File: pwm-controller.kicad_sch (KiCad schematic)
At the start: 41 parts, among them J1 DEBUG_ADDRESS_I2C_INT, J2 POWER, J3 OUT+, J4 OUT-, SW1 EC12D1524403, U1 STM8S003F3Px, U2 78L05

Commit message: order files
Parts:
- renumbered C4 to C1, C14 to C10, C5 to C2, C7 to C4, C8 to C5, C9 to C6, C2 to C7, C1 to C8, C6 to C9, D2 to D1, D1 to D2, H4 to H2, H2 to H3, H5 to H4, H7 to H5, H3 to H6, H6 to H7, J2 to J1, J1 to J2, R8 to R1, R7 to R10, R21 to R11, R10 to R2, R5 to R4, R9 to R5, R1 to R6, R2 to R7, R4 to R8, R6 to R9, U2 to U1, U1 to U2

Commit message: rendered some docs
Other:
- title: (none) -> Dual-channel PWM LED-strip controller
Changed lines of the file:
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@@
 (kicad_sch (version 20211123) (generator eeschema)
   (paper "A4")
+  (title_block
+    (title "Dual-channel PWM LED-strip controller")
+  )
   (junction (at 113.03 95.25) (diameter 0) (color 0 0 0 0)
   )

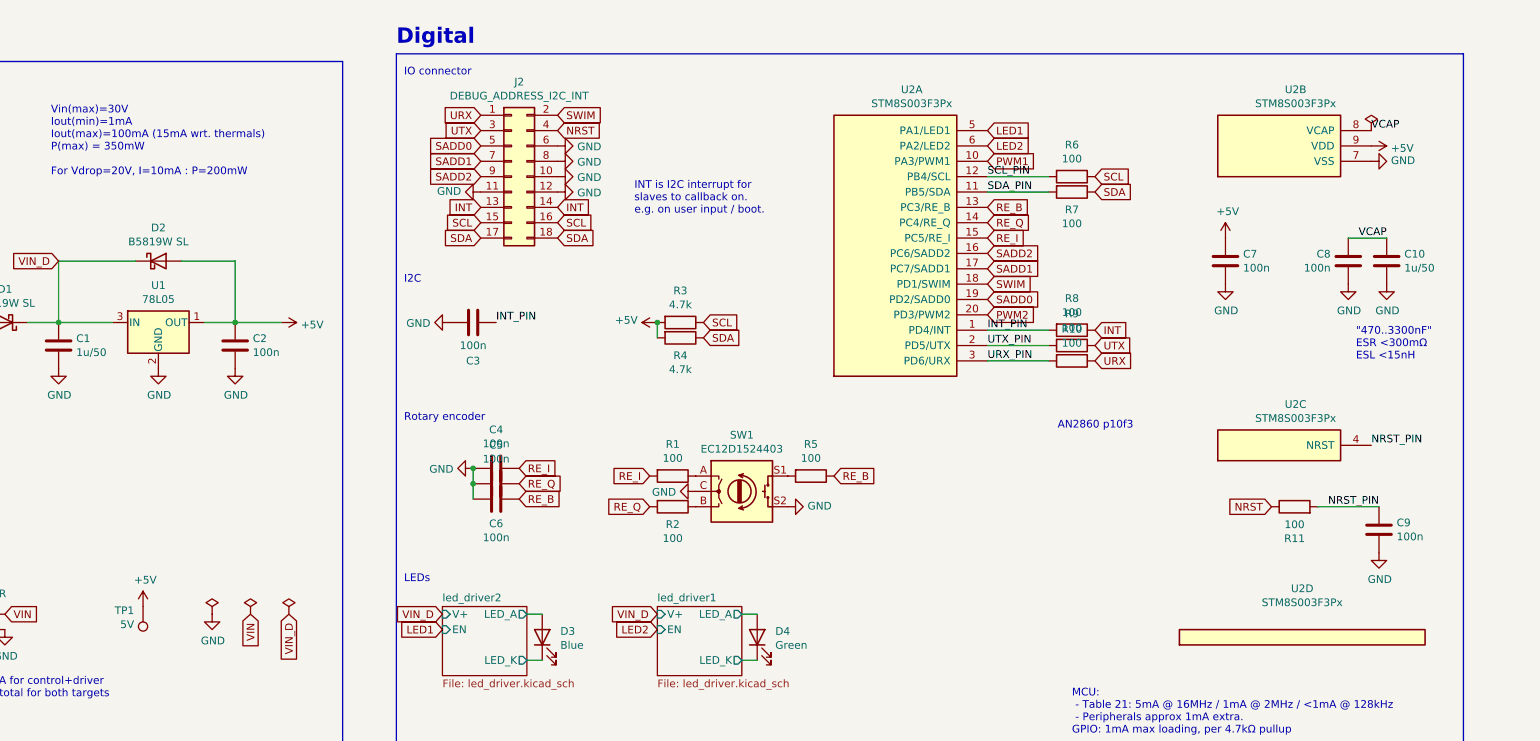
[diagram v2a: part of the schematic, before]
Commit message: fix rotary pinout, add 5v0 to header in extra-col, regen fab+doc
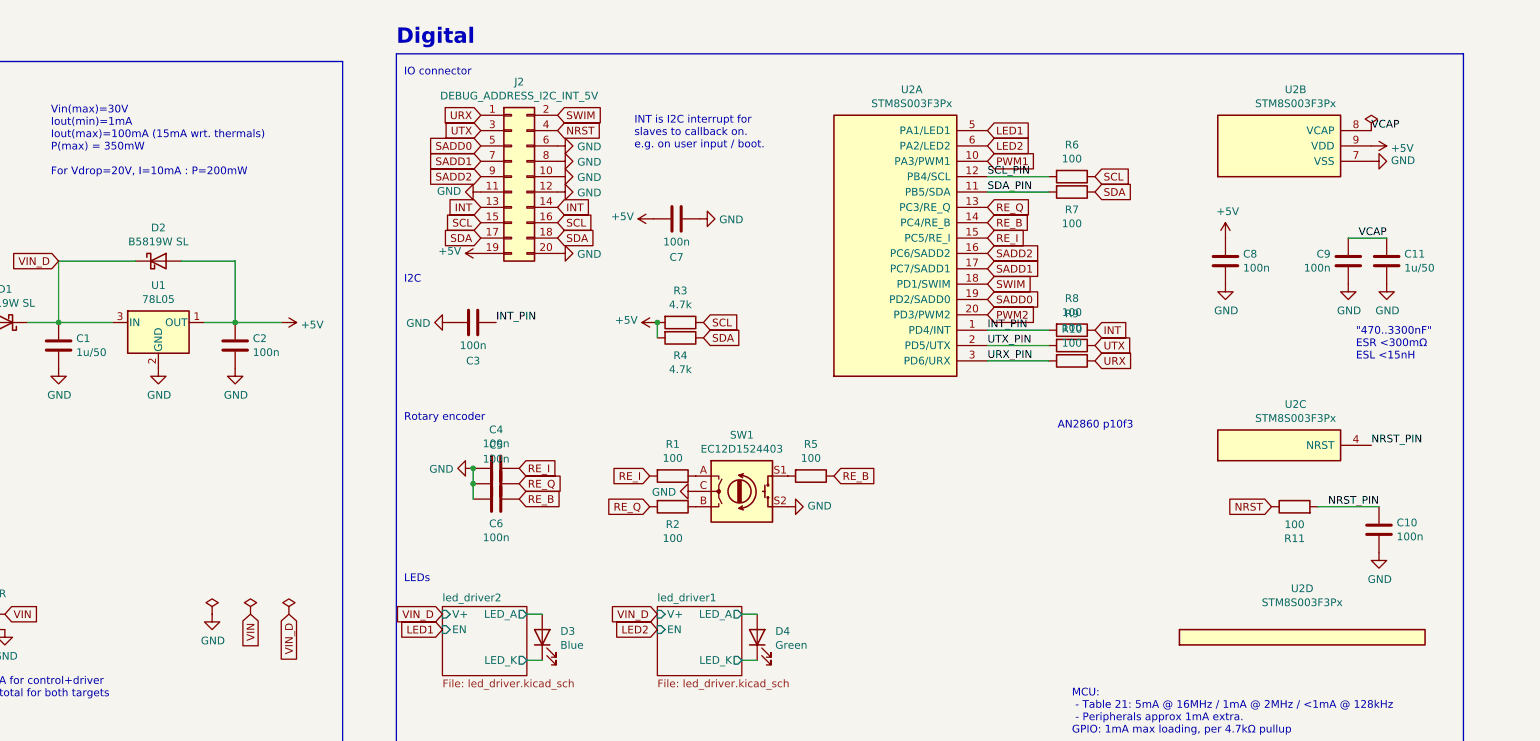
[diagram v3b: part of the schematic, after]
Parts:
- removed TP1: 5V, TestPoint:TestPoint_THTPad_D1.5mm_Drill0.7mm, symbol Connector:TestPoint
- added C7: 100n, Capacitor_SMD:C_0402_1005Metric, symbol Device:C
- J2: value DEBUG_ADDRESS_I2C_INT -> DEBUG_ADDRESS_I2C_INT_5V; footprint Connector_PinHeader_2.54mm:PinHeader_2x09_P2.54mm_Horizontal -> Connector_PinHeader_2.54mm:PinHeader_2x10_P2.54mm_Horizontal; symbol Connector_Generic:Conn_02x09_Odd_Even -> Connector_Generic:Conn_02x10_Odd_Even; JLC C492437 -> C492438
- renumbered C9 to C10, C10 to C11, C7 to C8, C8 to C9
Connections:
- net +5V: now also J2.19 (Pin_19), C7.1
- net GND: now also J2.20 (Pin_20), C7.2
- net RE_B: now also U2.14 (PC4/RE_B); no longer U2.13 (PC3/RE_B)
- net RE_Q: now also U2.13 (PC3/RE_Q); no longer U2.14 (PC4/RE_Q)

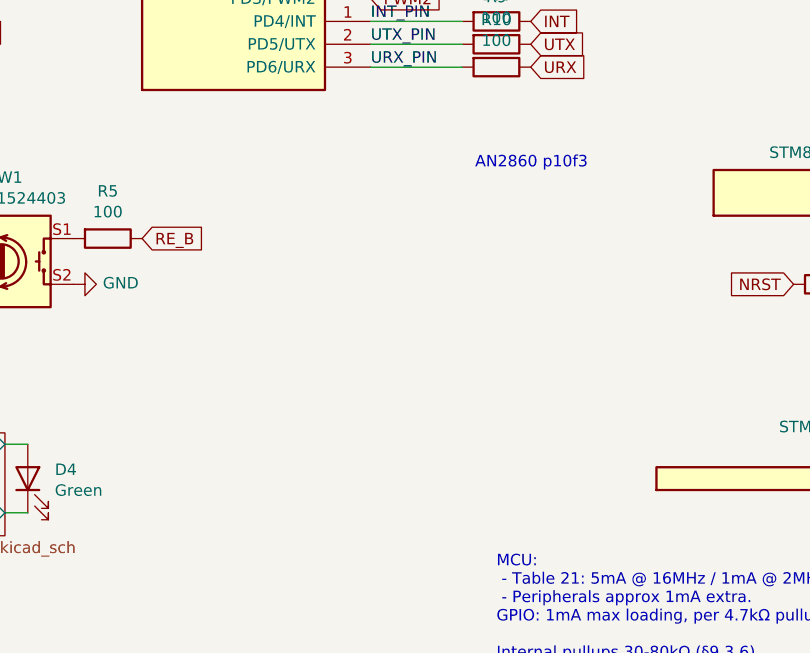
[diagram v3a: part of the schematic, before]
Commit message: TVS diodes added to I2C SDA+SCL+INT pins, renamed 1-/2- to A-/B-
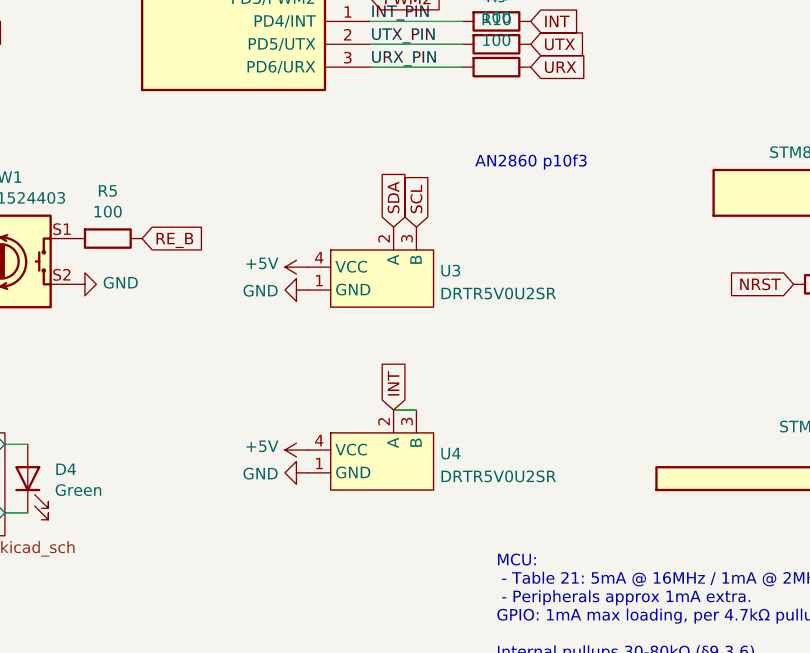
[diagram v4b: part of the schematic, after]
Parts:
- added U3, U4: DRTR5V0U2SR, Package_TO_SOT_SMD:SOT-143, symbol mark:DRTR5V0U2SR
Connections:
- net +5V: now also U3.4 (VCC), U4.4 (VCC)
- net GND: now also U3.1 (GND), U4.1 (GND)
- net INT: now also U4.2 (A), U4.3 (B)
- net SCL: now also U3.3 (B)
- net SDA: now also U3.2 (A)

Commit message: improvements, notes for future TODO stuff
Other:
- note added: "- ISO1540 to isolate I2C (need BUSPWR and BUSGND pins on connector) - Opto-isolator for INT? Perhaps move I2C+INT+BUSPWR+BUSGND to a pair of 5-pin JST connectors?"
- note added: "Should we add LC on input? 10A @ 1kHz : Q < 10 mC/cycle C=Q/V @ 12V : >1000μF L=1/(C 4π² f²) @ 1kHz & 1000uF : > 25μH Examples at bare-min spec: L = Bourns SRP1770C-330M (33μH, 18x17mm, €4) C = UC EKYC500ELL122ML20S (1200μF, 38mΩ, €2) L = Bourns SRP1265C-6R8M (6.8μH, 14x13mm, €2) C = Cornell SLPX103M050E7P3 (10mF, 46mΩ, €5) Ideally, we over-spec though, since capacitor discharge is not flat like 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"
- moved on the sheet: J1
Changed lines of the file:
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@@
+    (effects (font (size 1.27 1.27)) (justify left bottom))
+  )
+  (text "Should we add LC on input?\n\n10A @ 1kHz : Q < 10 mC/cycle\n\nC=Q/V @ 12V : >1000μF\n\nL=1/(C 4π² f²) @ 1kHz & 1000uF : > 25μH\n\nExamples at bare-min spec:\n\nL = Bourns SRP1770C-330M (33μH, 18x17mm, €4)\nC = UC EKYC500ELL122ML20S (1200μF, 38mΩ, €2)\n\nL = Bourns SRP1265C-6R8M (6.8μH, 14x13mm, €2)\nC = Cornell SLPX103M050E7P3 (10mF, 46mΩ, €5)\n\nIdeally, we over-spec though, since capacitor discharge is not flat like LiPo..."
+    (at -87.63 118.745 0)
+    (effects (font (size 1.27 1.27)) (justify left bottom))
+  )
+  (text " - ISO1540 to isolate I2C (need BUSPWR and BUSGND pins on connector)\n - Opto-isolator for INT?\n\nPerhaps move I2C+INT+BUSPWR+BUSGND to a pair of 5-pin JST connectors?"
+    (at 300.99 111.125 0)
     (effects (font (size 1.27 1.27)) (justify left bottom))
   )
@@
   )
   (text "<10mA for control+driver\n<15A total for both targets"
-    (at 29.21 130.81 0)
+    (at 29.21 113.665 0)
     (effects (font (size 1.27 1.27)) (justify left bottom))
   )
@@
     )
   )
-  (global_label "VIN_D" (shape input) (at 82.55 116.84 270) (fields_autoplaced)
-    (effects (font (size 1.27 1.27)) (justify right))
-    (property "Intersheet References" "${INTERSHEET_REFS}" (id 0) (at 0 0 0)
+  (global_label "VIN_D" (shape input) (at 82.55 99.695 270) (fields_autoplaced)
+    (effects (font (size 1.27 1.27)) (justify right))
+    (property "Intersheet References" "${INTERSHEET_REFS}" (id 0) (at 0 -17.145 0)
       (effects (font (size 1.27 1.27)) hide)
     )
@@
     )
   )
-  (global_label "VIN" (shape input) (at 76.2 116.84 270) (fields_autoplaced)
-    (effects (font (size 1.27 1.27)) (justify right))
-    (property "Intersheet References" "${INTERSHEET_REFS}" (id 0) (at 0 0 0)
+  (global_label "VIN" (shape input) (at 76.2 99.695 270) (fields_autoplaced)
+    (effects (font (size 1.27 1.27)) (justify right))
+    (property "Intersheet References" "${INTERSHEET_REFS}" (id 0) (at 0 -17.145 0)
       (effects (font (size 1.27 1.27)) hide)
     )
@@
     )
   )
-  (global_label "VIN" (shape input) (at 35.56 116.84 0) (fields_autoplaced)
-    (effects (font (size 1.27 1.27)) (justify left))
-    (property "Intersheet References" "${INTERSHEET_REFS}" (id 0) (at 0 0 0)
+  (global_label "VIN" (shape input) (at 35.56 99.695 0) (fields_autoplaced)
+    (effects (font (size 1.27 1.27)) (justify left))
+    (property "Intersheet References" "${INTERSHEET_REFS}" (id 0) (at 0 -17.145 0)
       (effects (font (size 1.27 1.27)) hide)
     )
@@
     (pin "2")
   )
-  (symbol (lib_id "power:PWR_FLAG") (at 76.2 116.84 0) (unit 1)
-    (in_bom yes) (on_board yes)
-    (property "Reference" "#FLG02" (id 0) (at 76.2 114.935 0)
-      (effects (font (size 1.27 1.27)) hide)
-    )
-    (property "Value" "PWR_FLAG" (id 1) (at 76.2 112.4458 0)
-      (effects (font (size 1.27 1.27)) hide)
-    )
-    (property "Footprint" "" (id 2) (at 76.2 116.84 0)
-      (effects (font (size 1.27 1.27)) hide)
-    )
-    (property "Datasheet" "~" (id 3) (at 76.2 116.84 0)
+  (symbol (lib_id "power:PWR_FLAG") (at 76.2 99.695 0) (unit 1)
+    (in_bom yes) (on_board yes)
+    (property "Reference" "#FLG02" (id 0) (at 76.2 97.79 0)
+      (effects (font (size 1.27 1.27)) hide)
+    )
+    (property "Value" "PWR_FLAG" (id 1) (at 76.2 95.3008 0)
+      (effects (font (size 1.27 1.27)) hide)
+    )
+    (property "Footprint" "" (id 2) (at 76.2 99.695 0)
+      (effects (font (size 1.27 1.27)) hide)
+    )
+    (property "Datasheet" "~" (id 3) (at 76.2 99.695 0)
       (effects (font (size 1.27 1.27)) hide)
     )
@@
     (pin "1")
   )
-  (symbol (lib_id "power:PWR_FLAG") (at 69.85 116.84 0) (unit 1)
-    (in_bom yes) (on_board yes)
-    (property "Reference" "#FLG01" (id 0) (at 69.85 114.935 0)
-      (effects (font (size 1.27 1.27)) hide)
-    )
-    (property "Value" "PWR_FLAG" (id 1) (at 69.85 112.4458 0)
-      (effects (font (size 1.27 1.27)) hide)
-    )
-    (property "Footprint" "" (id 2) (at 69.85 116.84 0)
-      (effects (font (size 1.27 1.27)) hide)
-    )
-    (property "Datasheet" "~" (id 3) (at 69.85 116.84 0)
+  (symbol (lib_id "power:PWR_FLAG") (at 69.85 99.695 0) (unit 1)
+    (in_bom yes) (on_board yes)
+    (property "Reference" "#FLG01" (id 0) (at 69.85 97.79 0)
+      (effects (font (size 1.27 1.27)) hide)
+    )
+    (property "Value" "PWR_FLAG" (id 1) (at 69.85 95.3008 0)
+      (effects (font (size 1.27 1.27)) hide)
+    )
+    (property "Footprint" "" (id 2) (at 69.85 99.695 0)
+      (effects (font (size 1.27 1.27)) hide)
+    )
+    (property "Datasheet" "~" (id 3) (at 69.85 99.695 0)
       (effects (font (size 1.27 1.27)) hide)
     )
@@
     (pin "1")
   )
-  (symbol (lib_id "power:GND") (at 69.85 116.84 0) (unit 1)
-    (in_bom yes) (on_board yes)
-    (property "Reference" "#PWR04" (id 0) (at 69.85 123.19 0)
-      (effects (font (size 1.27 1.27)) hide)
-    )
-    (property "Value" "GND" (id 1) (at 69.977 121.2342 0))
-    (property "Footprint" "" (id 2) (at 69.85 116.84 0)
-      (effects (font (size 1.27 1.27)) hide)
-    )
-    (property "Datasheet" "" (id 3) (at 69.85 116.84 0)
+  (symbol (lib_id "power:GND") (at 69.85 99.695 0) (unit 1)
+    (in_bom yes) (on_board yes)
+    (property "Reference" "#PWR04" (id 0) (at 69.85 106.045 0)
+      (effects (font (size 1.27 1.27)) hide)
+    )
+    (property "Value" "GND" (id 1) (at 69.977 104.0892 0))
+    (property "Footprint" "" (id 2) (at 69.85 99.695 0)
+      (effects (font (size 1.27 1.27)) hide)
+    )
+    (property "Datasheet" "" (id 3) (at 69.85 99.695 0)
       (effects (font (size 1.27 1.27)) hide)
     )
@@
     (pin "1")
   )
-  (symbol (lib_id "Connector:Screw_Terminal_01x02") (at 30.48 119.38 180) (unit 1)
-    (in_bom yes) (on_board yes)
-    (property "Reference" "J1" (id 0) (at 32.5628 111.125 0))
-    (property "Value" "POWER" (id 1) (at 32.5628 113.4364 0))
-    (property "Footprint" "mark:ScrewTerminal_5.08P_1x02_10.16x10.16mm" (id 2) (at 30.48 119.38 0)
-      (effects (font (size 1.27 1.27)) hide)
-    )
-    (property "Datasheet" "https://datasheet.lcsc.com/lcsc/1912251636_Ningbo-Kangnex-Elec-WJ500V-5.08-2P_C8465.pdf" (id 3) (at 30.48 119.38 0)
-      (effects (font (size 1.27 1.27)) hide)
-    )
-    (property "JLC" "C8465" (id 4) (at 30.48 119.38 0)
-      (effects (font (size 1.27 1.27)) hide)
-    )
-    (pin "1")
-    (pin "2")
-  )
-  (symbol (lib_id "power:GND") (at 35.56 119.38 0) (unit 1)
-    (in_bom yes) (on_board yes)
-    (property "Reference" "#PWR01" (id 0) (at 35.56 125.73 0)
-      (effects (font (size 1.27 1.27)) hide)
-    )
-    (property "Value" "GND" (id 1) (at 35.687 123.7742 0))
-    (property "Footprint" "" (id 2) (at 35.56 119.38 0)
-      (effects (font (size 1.27 1.27)) hide)
-    )
-    (property "Datasheet" "" (id 3) (at 35.56 119.38 0)
+  (symbol (lib_id "Connector:Screw_Terminal_01x02") (at 30.48 102.235 180) (unit 1)
+    (in_bom yes) (on_board yes)
+    (property "Reference" "J1" (id 0) (at 32.5628 93.98 0))
+    (property "Value" "POWER" (id 1) (at 32.5628 96.2914 0))
+    (property "Footprint" "mark:ScrewTerminal_5.08P_1x02_10.16x10.16mm" (id 2) (at 30.48 102.235 0)
+      (effects (font (size 1.27 1.27)) hide)
+    )
+    (property "Datasheet" "https://datasheet.lcsc.com/lcsc/1912251636_Ningbo-Kangnex-Elec-WJ500V-5.08-2P_C8465.pdf" (id 3) (at 30.48 102.235 0)
+      (effects (font (size 1.27 1.27)) hide)
+    )
+    (property "JLC" "C8465" (id 4) (at 30.48 102.235 0)
+      (effects (font (size 1.27 1.27)) hide)
+    )
+    (pin "1")
+    (pin "2")
+  )
+  (symbol (lib_id "power:GND") (at 35.56 102.235 0) (unit 1)
+    (in_bom yes) (on_board yes)
+    (property "Reference" "#PWR01" (id 0) (at 35.56 108.585 0)
+      (effects (font (size 1.27 1.27)) hide)
+    )
+    (property "Value" "GND" (id 1) (at 35.687 106.6292 0))
+    (property "Footprint" "" (id 2) (at 35.56 102.235 0)
+      (effects (font (size 1.27 1.27)) hide)
+    )
+    (property "Datasheet" "" (id 3) (at 35.56 102.235 0)
       (effects (font (size 1.27 1.27)) hide)
     )
@@
     (pin "2")
   )
-  (symbol (lib_id "power:PWR_FLAG") (at 82.55 116.84 0) (unit 1)
-    (in_bom yes) (on_board yes)
-    (property "Reference" "#FLG03" (id 0) (at 82.55 114.935 0)
-      (effects (font (size 1.27 1.27)) hide)
-    )
-    (property "Value" "PWR_FLAG" (id 1) (at 82.55 112.4458 0)
-      (effects (font (size 1.27 1.27)) hide)
-    )
-    (property "Footprint" "" (id 2) (at 82.55 116.84 0)
-      (effects (font (size 1.27 1.27)) hide)
-    )
-    (property "Datasheet" "~" (id 3) (at 82.55 116.84 0)
-      (effects (font (size 1.27 1.27)) hide)
-    )
+  (symbol (lib_id "power:PWR_FLAG") (at 82.55 99.695 0) (unit 1)
+    (in_bom yes) (on_board yes)
+    (property "Reference" "#FLG03" (id 0) (at 82.55 97.79 0)
+      (effects (font (size 1.27 1.27)) hide)
+    )
+    (property "Value" "PWR_FLAG" (id 1) (at 82.55 95.3008 0)
+      (effects (font (size 1.27 1.27)) hide)
+    )
+    (property "Footprint" "" (id 2) (at 82.55 99.695 0)
+      (effects (font (size 1.27 1.27)) hide)
+    )
+    (property "Datasheet" "~" (id 3) (at 82.55 99.695 0)
+      (effects (font (size 1.27 1.27)) hide)
+    )
